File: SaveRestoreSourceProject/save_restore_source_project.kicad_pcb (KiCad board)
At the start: 2 copper layers, 79 parts

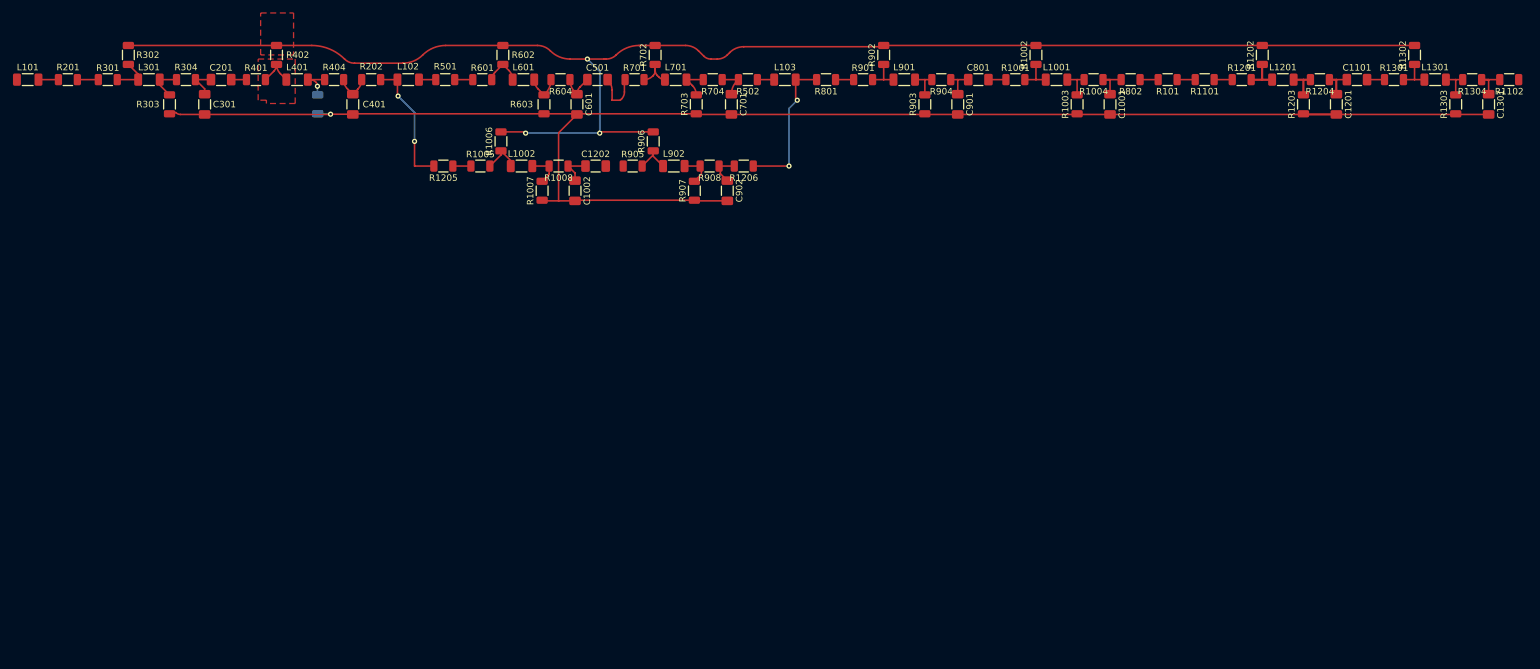
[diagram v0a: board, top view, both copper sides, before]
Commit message: Add support for connected drawings, update test template
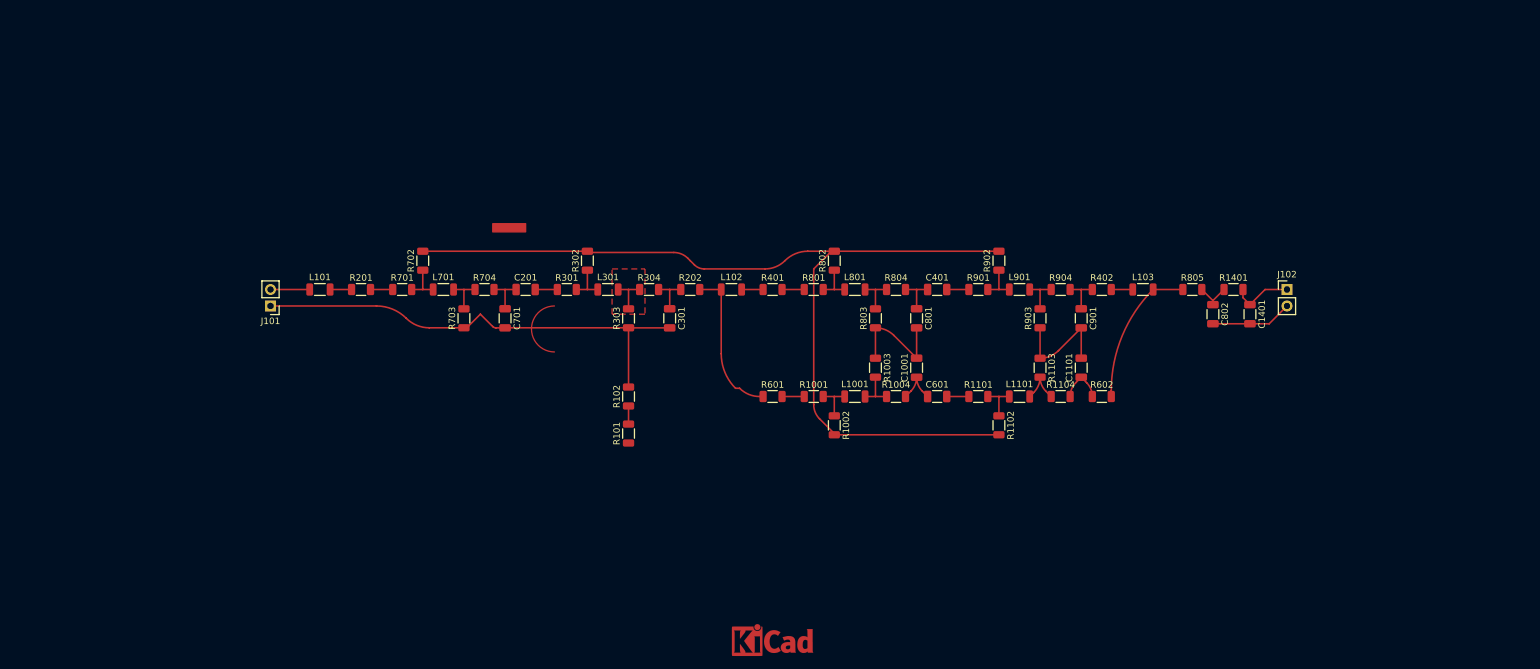
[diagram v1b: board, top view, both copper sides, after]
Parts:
- removed C1002, C1201, C1202, C1301, C501, C902: 100n, Capacitor_SMD:C_1206_3216Metric_Pad1.33x1.80mm_HandSolder
- removed L1002, L1201, L1301, L401, L601, L902: 10uH, Inductor_SMD:L_1206_3216Metric_Pad1.22x1.90mm_HandSolder
- removed R1005, R1008, R1201, R1204, R1205, R1206, R1301, R1304, R404, R501, R502, R604, R905, R908: 1k, Resistor_SMD:R_1206_3216Metric
- removed R1006, R1202, R1302, R906: 4k7, Resistor_SMD:R_1206_3216Metric
- removed R1007, R1203, R1303, R403, R603, R907: 2k2, Resistor_SMD:R_1206_3216Metric
- added C1401: C, Capacitor_SMD:C_1206_3216Metric, F.Cu at (214.6, 73.7)
- added C802: C, Capacitor_SMD:C_1206_3216Metric, F.Cu at (208.9, 73.7)
- added J101: Conn_01x02, Connector_PinHeader_2.54mm:PinHeader_1x02_P2.54mm_Vertical, F.Cu at (63.5, 72.4)
- added J102: Conn_01x02, Connector_PinHeader_2.54mm:PinHeader_1x02_P2.54mm_Vertical, F.Cu at (220.3, 69.8)
- added L1101: L, Inductor_SMD:L_1206_3216Metric, F.Cu at (179.1, 86.4)
- added L801: L, Inductor_SMD:L_1206_3216Metric, F.Cu at (153.7, 69.8)
- added R102: R, Resistor_SMD:R_1206_3216Metric, F.Cu at (118.7, 86.4)
- added R1103: R, Resistor_SMD:R_1206_3216Metric, F.Cu at (182.2, 81.9)
- added R1104: R, Resistor_SMD:R_1206_3216Metric, F.Cu at (185.4, 86.4)
- added R1401: R, Resistor_SMD:R_1206_3216Metric, F.Cu at (212.1, 69.8)
- added R803: R, Resistor_SMD:R_1206_3216Metric, F.Cu at (156.8, 74.3)
- added R804: R, Resistor_SMD:R_1206_3216Metric, F.Cu at (160.0, 69.8)
- added R805: R, Resistor_SMD:R_1206_3216Metric, F.Cu at (205.7, 69.8)
- added REF**: KiCad-Logo_5mm_Copper, Symbol:KiCad-Logo_5mm_Copper, F.Cu at (141.0, 124.5)
- C1001, C1101, C201, C301, C401, C601, C701, C801, C901: value 100n -> C; footprint Capacitor_SMD:C_1206_3216Metric_Pad1.33x1.80mm_HandSolder -> Capacitor_SMD:C_1206_3216Metric
- L1001, L101, L102, L103, L301, L701, L901: value 10uH -> L; footprint Inductor_SMD:L_1206_3216Metric_Pad1.22x1.90mm_HandSolder -> Inductor_SMD:L_1206_3216Metric
- R1001, R1004, R101, R1101, R1102, R201, R202, R301, R304, R401, R601, R701, R704, R801, R802, R901, R904: value 1k -> R
- R1002, R302, R402, R602, R702, R902: value 4k7 -> R
- R1003, R303, R703, R903: value 2k2 -> R
- moved R402 132.4 mm to (191.8, 69.8), turned to 0 degrees
- moved R602 106.4 mm to (191.8, 86.4), turned to 0 degrees
- moved R101 99.5 mm to (118.7, 92.1), turned to 90 degrees
- moved R1102 95.1 mm to (175.9, 90.8), turned to -90 degrees
- moved C401 94.6 mm to (166.4, 69.8), turned to 0 degrees
- moved R401 86.0 mm to (141.0, 69.8)
- moved C301 79.0 mm to (125.1, 74.3)
- moved R304 78.5 mm to (121.9, 69.8), turned to 0 degrees
- moved R303 78.1 mm to (118.7, 74.3)
- moved L301 77.9 mm to (115.6, 69.8)
- moved R301 77.9 mm to (109.2, 69.8)
- moved R302 77.6 mm to (112.4, 65.4)
- moved C601 71.6 mm to (166.4, 86.4), turned to 0 degrees
- moved R601 66.3 mm to (141.0, 86.4)
- moved R1002 65.1 mm to (150.5, 90.8), turned to -90 degrees
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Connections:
- C1001 pad 1: /relative_1_a/relative_2_b/out -> /mezzanine/local_mezzanine/local_2_a1/out
- C1101 pad 1: /relative_1_a1/relative_2_a/out -> /mezzanine/local_mezzanine/local_2_b1/out
- C1101 pad 2: /relative_1_a1/relative_2_b/in -> GND
- C301 pad 1: /local_1_a/local_2_a/out -> /local_1_a/local_2_b/out
- C401 pad 1: /local_1_a/local_2_b/out -> /local_1_b/local_2_a/out
- C401 pad 2: GND -> /local_1_b/local_2_b/in
- C601 pad 1: /local_1_b/local_2_a/out -> /mezzanine/local_mezzanine/local_2_a1/out
- C601 pad 2: GND -> /mezzanine/local_mezzanine/local_2_b1/in
- C701 pad 1: /local_1_b/local_2_b/out -> /local_1_a/local_2_a/out
- C801 pad 1: /relative_1_a/relative_2_a/out -> /local_1_b/local_2_a/out
- C801 pad 2: /relative_1_a/relative_2_b/in -> GND
- C901 pad 1: /relative_1_a/relative_2_a/out -> /local_1_b/local_2_b/out
- L1001 pad 2: Net-(L1001-Pad2) -> /mezzanine/local_mezzanine/local_2_a1/mid
- L101 pad 1: unconnected-(L101-Pad1) -> Net-(J101-Pin_2)
- L301 pad 2: Net-(L301-Pad2) -> /local_1_a/local_2_b/mid
- L701 pad 2: Net-(L701-Pad2) -> /local_1_a/local_2_a/mid
- L901 pad 2: Net-(L901-Pad2) -> /local_1_b/local_2_b/mid
- R1001 pad 1: /relative_1_a/relative_2_b/in -> /mezzanine/local_mezzanine/local_2_a1/in
- R1003 pad 2: Net-(L1001-Pad2) -> /mezzanine/local_mezzanine/local_2_a1/mid
- R1004 pad 1: /relative_1_a/relative_2_b/out -> /mezzanine/local_mezzanine/local_2_a1/mid
- R1004 pad 2: Net-(L1001-Pad2) -> /mezzanine/local_mezzanine/local_2_a1/out
- R101 pad 1: /relative_1_a1/in -> +12V
- R101 pad 2: /relative_1_a/out -> Net-(R101-Pad2)
- R1101 pad 1: /relative_1_a1/relative_2_a/in -> /mezzanine/local_mezzanine/local_2_b1/in
- R1101 pad 2: /relative_1_a1/in -> Net-(L1101-Pad1)
- R1102 pad 1: /relative_1_a1/out -> Net-(L1101-Pad1)
- R1102 pad 2: /relative_1_a1/relative_2_b/out -> +5V
- R201 pad 1: /local_1_a/local_2_a/in -> /local_1_a/in
- R201 pad 2: /local_1_a/in -> /local_1_a/local_2_a/in
- R202 pad 1: /local_1_a/out -> /local_1_a/local_2_b/out
- R202 pad 2: /local_1_a/local_2_b/out -> /local_1_a/out
- R301 pad 1: /local_1_a/local_2_a/in -> /local_1_a/local_2_b/in
- R303 pad 2: Net-(L301-Pad2) -> /local_1_a/local_2_b/mid
- R304 pad 1: /local_1_a/local_2_a/out -> /local_1_a/local_2_b/mid
- R304 pad 2: Net-(L301-Pad2) -> /local_1_a/local_2_b/out
- R401 pad 1: /local_1_a/local_2_b/in -> /local_1_b/in
- R401 pad 2: Net-(L401-Pad1) -> /local_1_b/local_2_a/in
- R402 pad 1: Net-(L401-Pad1) -> /local_1_b/local_2_b/out
- R402 pad 2: +5V -> /local_1_b/out
- R601 pad 1: /local_1_b/local_2_a/in -> /local_1_a/out
- R601 pad 2: Net-(L601-Pad1) -> /mezzanine/local_mezzanine/local_2_a1/in
- R602 pad 1: Net-(L601-Pad1) -> /mezzanine/local_mezzanine/local_2_b1/out
- R602 pad 2: +5V -> /mezzanine/out
- R701 pad 1: /local_1_b/local_2_b/in -> /local_1_a/local_2_a/in
- R703 pad 2: Net-(L701-Pad2) -> /local_1_a/local_2_a/mid
- R704 pad 1: /local_1_b/local_2_b/out -> /local_1_a/local_2_a/mid
- R704 pad 2: Net-(L701-Pad2) -> /local_1_a/local_2_a/out
- R801 pad 1: /relative_1_a/relative_2_a/in -> /local_1_b/local_2_a/in
- R801 pad 2: /mezzanine/out -> Net-(L801-Pad1)
- R802 pad 1: /relative_1_a/out -> Net-(L801-Pad1)
- R802 pad 2: /relative_1_a/relative_2_b/out -> +5V
- R901 pad 1: /relative_1_a/relative_2_a/in -> /local_1_b/local_2_b/in
- R903 pad 2: Net-(L901-Pad2) -> /local_1_b/local_2_b/mid
- R904 pad 1: /relative_1_a/relative_2_a/out -> /local_1_b/local_2_b/mid
- R904 pad 2: Net-(L901-Pad2) -> /local_1_b/local_2_b/out
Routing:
- net GND: track 254.9 -> 120.7 mm, vias 1 -> 0
- net +5V: track 239.1 -> 146.8 mm, vias 3 -> 0
- net Net-(L1201-Pad1): track 11.1 -> 0.00 mm
- net Net-(L1201-Pad2): track 9.88 -> 0.00 mm
- net /remote_2_a1/out: track 0.00 -> 9.46 mm
- net /relative_1_a1/relative_2_a/out: track 8.26 -> 0.00 mm
- net /mezzanine/local_mezzanine/local_2_b1/out: track 0.00 -> 7.07 mm
- net /mezzanine/local_mezzanine/local_2_a1/out: track 0.00 -> 7.06 mm
- net /mezzanine/local_mezzanine/local_2_b1/mid: track 0.00 -> 7.03 mm
- net Net-(L1101-Pad1): track 0.00 -> 6.30 mm
- net /mezzanine/local_mezzanine/local_2_a1/mid: track 0.00 -> 6.30 mm
- net /local_1_b/local_2_b/mid: track 0.00 -> 6.30 mm
- net /local_1_b/local_2_a/mid: track 0.00 -> 6.30 mm
- net /local_1_a/local_2_b/mid: track 0.00 -> 6.30 mm
- net /local_1_a/local_2_a/mid: track 0.00 -> 6.30 mm
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- added copper zone on F.Cu, net /local_1_a/local_2_b/mid
- removed copper zone on F.Cu, net +5V
- removed copper zone on F.Cu, net Net-(L401-Pad1)
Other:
- board text added: "test"
- board text removed: "A"
